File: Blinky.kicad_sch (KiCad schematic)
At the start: 26 parts, among them U4 LM331N, U5 LTV-817S, U6 TLP184

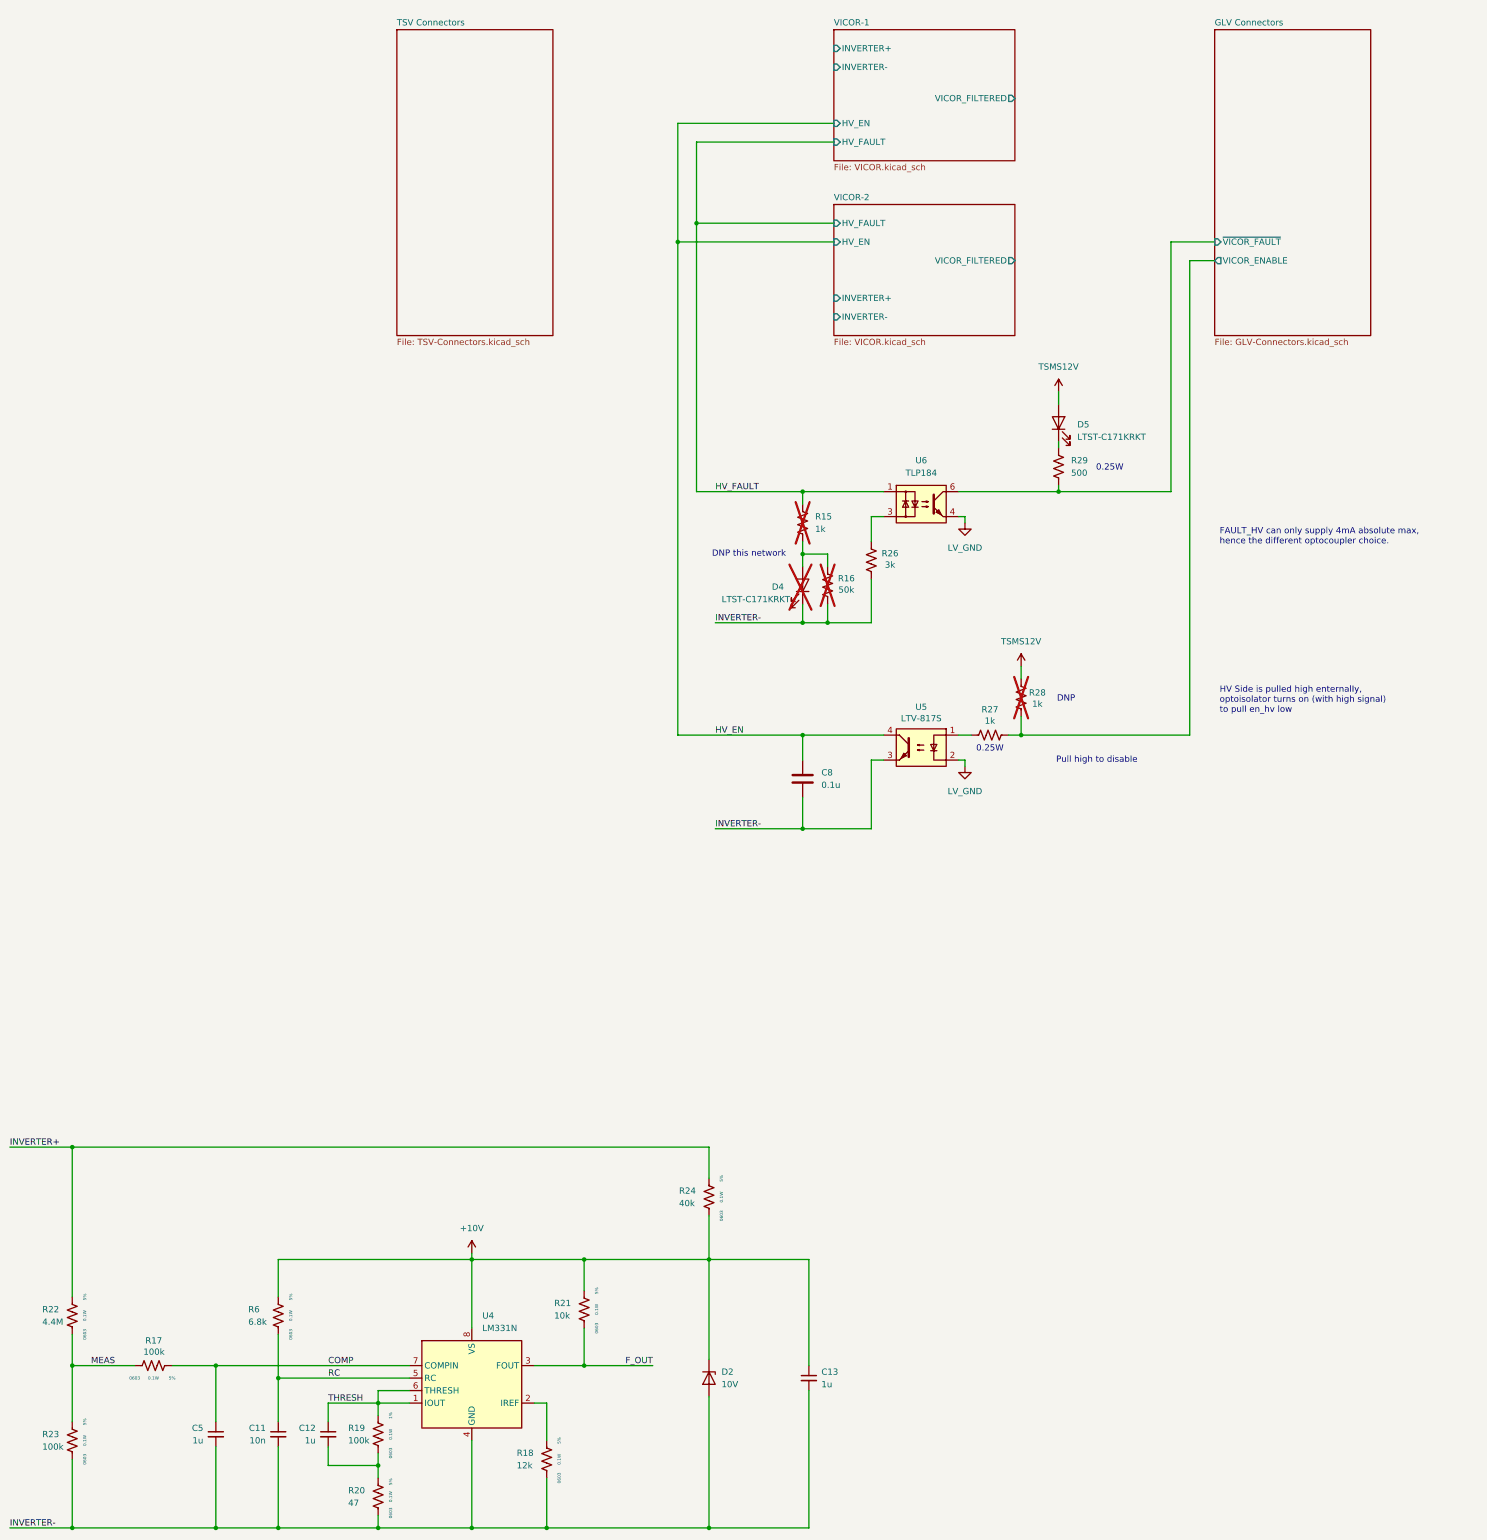
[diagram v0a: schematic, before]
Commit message: Finished up draft 1 of schematic
Need to look everything over and do a quick layout
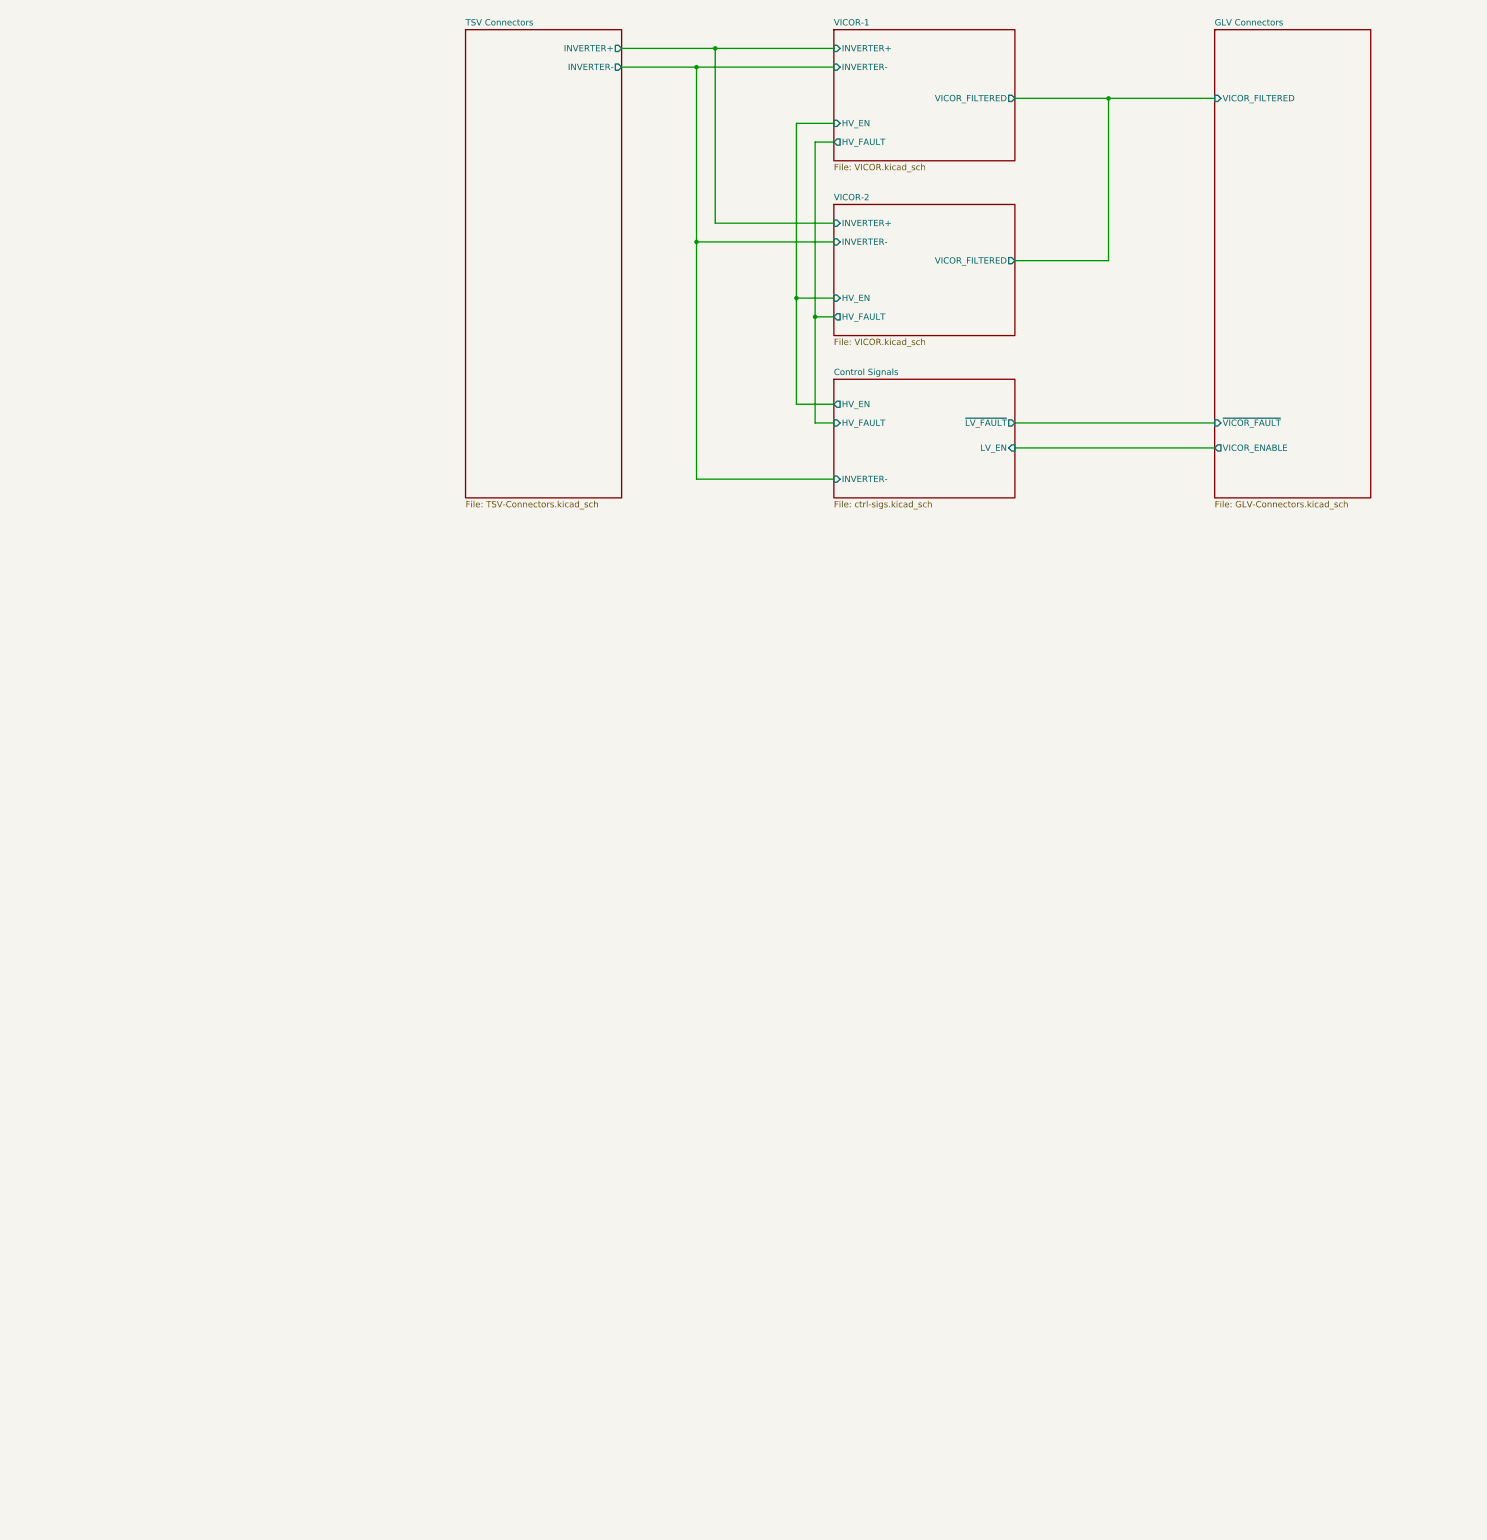
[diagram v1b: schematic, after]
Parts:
- removed C11: 10n, symbol Device:C_Small
- removed C12, C13, C5: 1u, symbol Device:C_Small
- removed C8: 0.1u, Capacitor_SMD:C_0603_1608Metric, symbol Device:C
- removed D2: 10V, symbol Device:D_Zener
- removed D4, D5: LTST-C171KRKT, LED_SMD:LED_0805_2012Metric, symbol Device:LED
- removed R15, R28: 1k, Resistor_SMD:R_0603_1608Metric_Pad0.98x0.95mm_HandSolder, symbol Device:R_US
- removed R16: 50k, Resistor_SMD:R_0603_1608Metric_Pad0.98x0.95mm_HandSolder, symbol Device:R_US
- removed R17, R19, R23: 100k, Resistor_SMD:R_0603_1608Metric_Pad0.98x0.95mm_HandSolder, symbol AERO_Resistors:R_0603
- removed R18: 12k, Resistor_SMD:R_0603_1608Metric_Pad0.98x0.95mm_HandSolder, symbol AERO_Resistors:R_0603
- removed R20: 47, Resistor_SMD:R_0603_1608Metric_Pad0.98x0.95mm_HandSolder, symbol AERO_Resistors:R_0603
- removed R21: 10k, Resistor_SMD:R_0603_1608Metric_Pad0.98x0.95mm_HandSolder, symbol AERO_Resistors:R_0603
- removed R22: 4.4M, Resistor_SMD:R_0603_1608Metric_Pad0.98x0.95mm_HandSolder, symbol AERO_Resistors:R_0603
- removed R24: 40k, Resistor_SMD:R_0603_1608Metric_Pad0.98x0.95mm_HandSolder, symbol AERO_Resistors:R_0603
- removed R26: 3k, Resistor_SMD:R_0603_1608Metric_Pad0.98x0.95mm_HandSolder, symbol Device:R_US
- removed R27: 1k, Resistor_SMD:R_0805_2012Metric_Pad1.20x1.40mm_HandSolder, symbol Device:R_US
- removed R29: 500, Resistor_SMD:R_0805_2012Metric_Pad1.20x1.40mm_HandSolder, symbol Device:R_US
- removed R6: 6.8k, Resistor_SMD:R_0603_1608Metric_Pad0.98x0.95mm_HandSolder, symbol AERO_Resistors:R_0603
- removed U4: LM331N, Package_DIP:DIP-8_W7.62mm, symbol Analog:LM331N
- removed U5: LTV-817S, Package_DIP:SMDIP-4_W9.53mm, symbol Isolator:LTV-817S
- removed U6: TLP184, Package_SO:Toshiba_SOIC-4-6_4.4x3.6mm_P1.27mm, symbol Isolator:TLP184
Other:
- added sheet Control Signals (ctrl-sigs.kicad_sch)
- sheet GLV Connectors ports: added VICOR_FILTERED; removed none
- sheet TSV Connectors ports: added INVERTER+, INVERTER-; removed none
- note removed: "0.25W"
- note removed: "DNP"
- note removed: "DNP this network"
- note removed: "FAULT_HV can only supply 4mA absolute max, hence the different optocoupler choice."
- note removed: "HV Side is pulled high enternally, optoisolator turns on (with high signal) to pull en_hv low"
- note removed: "Pull high to disable"

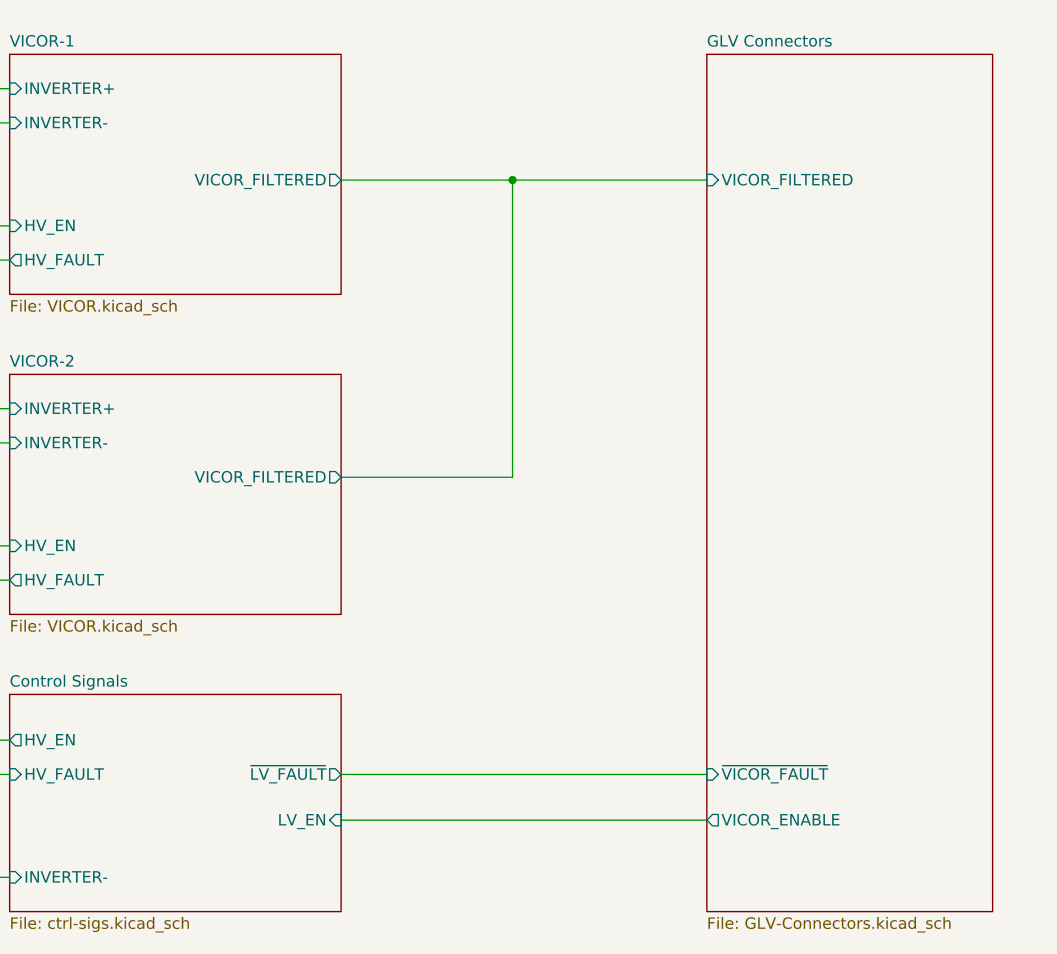
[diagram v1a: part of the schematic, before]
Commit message: Started layout
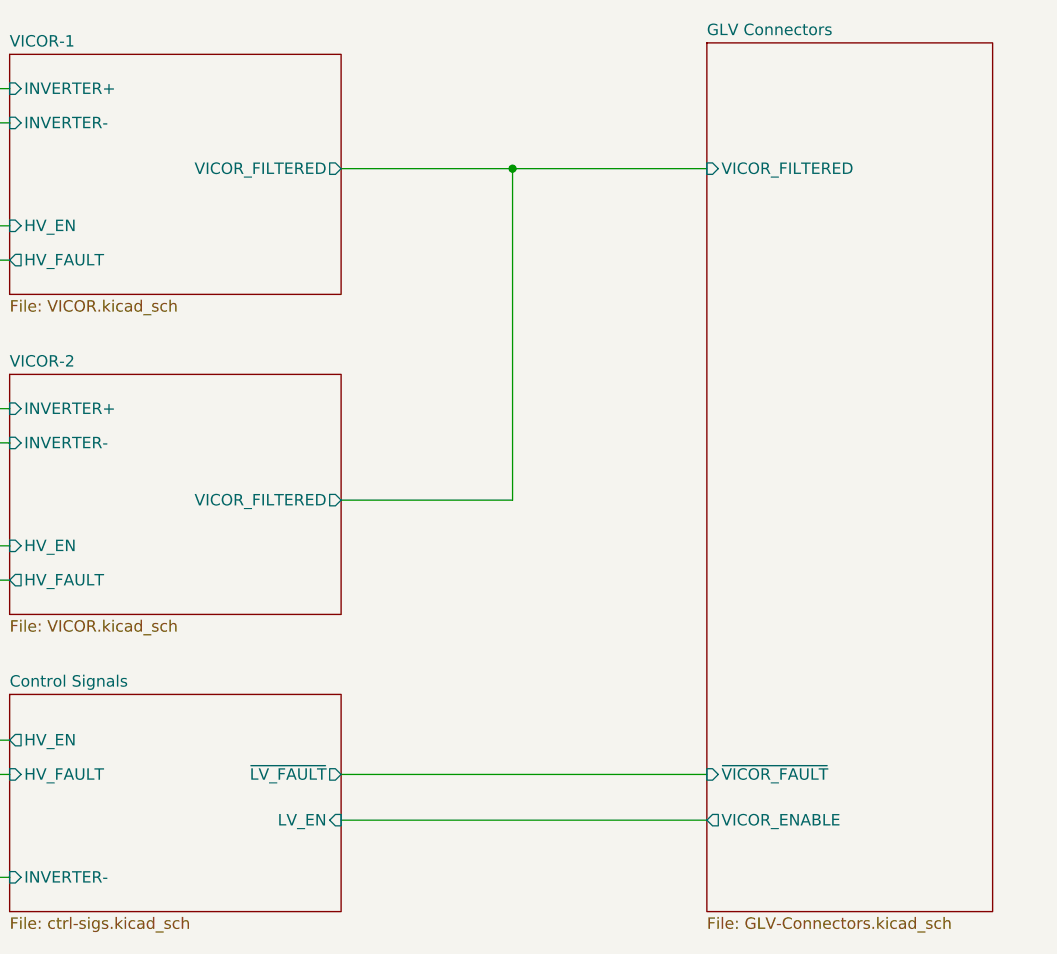
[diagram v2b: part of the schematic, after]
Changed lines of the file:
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@@
 	(paper "A3")
+	(junction
+		(at 260.35 93.98)
+		(diameter 0)
+		(color 0 0 0 0)
+	)
 	(junction
 		(at 176.53 124.46)
@@
 		(color 0 0 0 0)
 	)
-	(junction
-		(at 260.35 95.25)
-		(diameter 0)
-		(color 0 0 0 0)
-	)
 	(wire
 		(pts
@@
 	(wire
 		(pts
-			(xy 241.3 128.27) (xy 260.35 128.27)
-		)
-		(stroke
-			(width 0)
-			(type default)
-		)
-	)
-	(wire
-		(pts
-			(xy 260.35 95.25) (xy 281.94 95.25)
+			(xy 241.3 130.81) (xy 260.35 130.81)
+		)
+		(stroke
+			(width 0)
+			(type default)
+		)
+	)
+	(wire
+		(pts
+			(xy 260.35 93.98) (xy 281.94 93.98)
 		)
 		(stroke
@@
 	(wire
 		(pts
-			(xy 241.3 95.25) (xy 260.35 95.25)
+			(xy 241.3 93.98) (xy 260.35 93.98)
 		)
 		(stroke
@@
 	(wire
 		(pts
-			(xy 260.35 128.27) (xy 260.35 95.25)
+			(xy 260.35 93.98) (xy 260.35 130.81)
 		)
 		(stroke
@@
 		)
 		(pin "VICOR_FILTERED" output
-			(at 241.3 95.25 0)
+			(at 241.3 93.98 0)
 			(effects
 				(font
@@
 		)
 		(pin "VICOR_FILTERED" output
-			(at 241.3 128.27 0)
+			(at 241.3 130.81 0)
 			(effects
 				(font
@@
 	)
 	(sheet
-		(at 281.94 81.28)
-		(size 31.75 95.25)
+		(at 281.94 80.01)
+		(size 31.75 96.52)
 		(exclude_from_sim no)
 		(in_bom yes)
@@
 		)
 		(property "Sheetname" "GLV Connectors"
-			(at 281.94 80.5684 0)
+			(at 281.94 79.2984 0)
 			(show_name no)
 			(do_not_autoplace no)
@@
 		)
 		(pin "VICOR_FILTERED" input
-			(at 281.94 95.25 180)
-			(effects
-				(font
+			(at 281.94 93.98 180)
+			(effects
+				(font
